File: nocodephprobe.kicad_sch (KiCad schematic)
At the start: 34 parts, among them J1 RF1-01 BNC, J2 10K, Q1 2N7002, U1 LMV358a, U2 ICL7106CPL, U3 MCP1501T-10E/CHY, U4 VI-302-DP-RC-S, U5 L7805

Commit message: Transpose R6 and R7
In the prototype the voffset was 0.3V instead of 0.7V!
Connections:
- net GND: now also R7.1; no longer R6.1
- net Voffset: now also R6.1, R7.2; no longer R6.2, R7.1
- net Vref: now also R6.2; no longer R7.2
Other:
- moved on the sheet: R6, R7
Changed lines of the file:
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@@
   (junction (at 142.24 64.77) (diameter 0) (color 0 0 0 0)
   )
+  (junction (at 68.58 142.24) (diameter 0) (color 0 0 0 0)
+  )
   (junction (at 69.85 74.93) (diameter 0) (color 0 0 0 0)
   )
   (junction (at 66.04 63.5) (diameter 0) (color 0 0 0 0)
-  )
-  (junction (at 68.58 142.24) (diameter 0) (color 0 0 0 0)
   )
   (junction (at 275.59 90.17) (diameter 0) (color 0 0 0 0)
@@
     (stroke (width 0) (type default))
   )
-  (wire (pts (xy 68.58 142.24) (xy 68.58 144.78))
-    (stroke (width 0) (type default))
-  )
   (wire (pts (xy 147.32 77.47) (xy 142.24 77.47))
     (stroke (width 0) (type default))
@@
     (stroke (width 0) (type default))
   )
+  (wire (pts (xy 68.58 142.24) (xy 68.58 143.51))
+    (stroke (width 0) (type default))
+  )
   (wire (pts (xy 222.25 86.36) (xy 222.25 90.17))
     (stroke (width 0) (type default))
@@
     (stroke (width 0) (type default))
   )
+  (wire (pts (xy 68.58 151.13) (xy 68.58 152.4))
+    (stroke (width 0) (type default))
+  )
   (wire (pts (xy 217.17 76.2) (xy 227.33 76.2))
     (stroke (width 0) (type default))
@@
   )
   (wire (pts (xy 224.79 85.09) (xy 240.03 85.09))
-    (stroke (width 0) (type default))
-  )
-  (wire (pts (xy 68.58 140.97) (xy 68.58 142.24))
     (stroke (width 0) (type default))
   )
@@
     )
   )
-  (symbol (lib_id "Device:R_US") (at 68.58 148.59 180) (unit 1)
+  (symbol (lib_id "Device:R_US") (at 68.58 138.43 180) (unit 1)
     (in_bom yes) (on_board yes) (dnp no)
-    (property "Reference" "R6" (at 71.12 148.59 0)
-      (effects (font (size 1.27 1.27)) (justify right))
-    )
-    (property "Value" "4.64k" (at 71.12 151.13 0)
-      (effects (font (size 1.27 1.27)) (justify right))
-    )
-    (property "Footprint" "Resistor_SMD:R_0805_2012Metric_Pad1.20x1.40mm_HandSolder" (at 67.564 148.336 90)
-      (effects (font (size 1.27 1.27)) hide)
-    )
-    (property "Datasheet" "~" (at 68.58 148.59 0)
-      (effects (font (size 1.27 1.27)) hide)
-    )
-    (property "Tolerance" "0.1%" (at 73.66 153.67 0)
+    (property "Reference" "R6" (at 71.12 138.43 0)
+      (effects (font (size 1.27 1.27)) (justify right))
+    )
+    (property "Value" "4.64k" (at 71.12 140.97 0)
+      (effects (font (size 1.27 1.27)) (justify right))
+    )
+    (property "Footprint" "Resistor_SMD:R_0805_2012Metric_Pad1.20x1.40mm_HandSolder" (at 67.564 138.176 90)
+      (effects (font (size 1.27 1.27)) hide)
+    )
+    (property "Datasheet" "~" (at 68.58 138.43 0)
+      (effects (font (size 1.27 1.27)) hide)
+    )
+    (property "Tolerance" "0.1%" (at 73.66 143.51 0)
       (effects (font (size 1.27 1.27)))
     )
@@
     )
   )
-  (symbol (lib_id "Device:R_US") (at 68.58 137.16 180) (unit 1)
+  (symbol (lib_id "Device:R_US") (at 68.58 147.32 180) (unit 1)
     (in_bom yes) (on_board yes) (dnp no)
-    (property "Reference" "R7" (at 71.12 137.16 0)
-      (effects (font (size 1.27 1.27)) (justify right))
-    )
-    (property "Value" "10k" (at 71.12 139.7 0)
-      (effects (font (size 1.27 1.27)) (justify right))
-    )
-    (property "Footprint" "Resistor_SMD:R_0805_2012Metric_Pad1.20x1.40mm_HandSolder" (at 67.564 136.906 90)
-      (effects (font (size 1.27 1.27)) hide)
-    )
-    (property "Datasheet" "~" (at 68.58 137.16 0)
-      (effects (font (size 1.27 1.27)) hide)
-    )
-    (property "Tolerance" "0.1%" (at 77.47 139.7 0)
-      (effects (font (size 1.27 1.27)))
-    )
-    (property "Field5" "" (at 68.58 137.16 0)
-      (effects (font (size 1.27 1.27)) hide)
-    )
+    (property "Reference" "R7" (at 71.12 147.32 0)
+      (effects (font (size 1.27 1.27)) (justify right))
+    )
+    (property "Value" "10k" (at 71.12 149.86 0)
+      (effects (font (size 1.27 1.27)) (justify right))
+    )
+    (property "Footprint" "Resistor_SMD:R_0805_2012Metric_Pad1.20x1.40mm_HandSolder" (at 67.564 147.066 90)
+      (effects (font (size 1.27 1.27)) hide)
+    )
+    (property "Datasheet" "~" (at 68.58 147.32 0)
+      (effects (font (size 1.27 1.27)) hide)
+    )
+    (property "Tolerance" "0.1%" (at 77.47 149.86 0)
+      (effects (font (size 1.27 1.27)))
+    )
+    (property "Field5" "" (at 68.58 147.32 0)
+      (effects (font (size 1.27 1.27)) hide)
+    )

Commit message: schematic: add pn and datasheet to ntc
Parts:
- J2: foot print pn (none) -> STX-3120-3B; pn (none) -> USP10982
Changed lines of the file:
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@@
       (effects (font (size 1.27 1.27)) hide)
     )
-    (property "Datasheet" "~" (at 152.4 68.58 0)
+    (property "Datasheet" "https://www.littelfuse.com/~/media/electronics/datasheets/thermistor_probes_and_assemblies/littelfuse_thermistor_probes_assemblies_plastic_usp10982_datasheet.pdf.pdf" (at 152.4 68.58 0)
       (effects (font (size 1.27 1.27)) hide)
     )
+    (property "pn" "USP10982" (at 152.4 69.85 0)
+      (effects (font (size 1.27 1.27)) hide)
+    )
+    (property "foot print pn" "STX-3120-3B" (at 152.4 69.85 0)
+      (effects (font (size 1.27 1.27)) hide)
+    )
+    (property "Field6" "" (at 152.4 69.85 0)
+      (effects (font (size 1.27 1.27)) hide)
+    )

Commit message: Add decoupling caps to potentiometers
This also changes the 7805 to a smaller footprint
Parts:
- added C10, C12: 0.1uF, Capacitor_SMD:C_0805_2012Metric_Pad1.18x1.45mm_HandSolder, symbol Device:C
- U5: value L7805 -> 78l05; footprint Package_TO_SOT_SMD:TO-252-3_TabPin2 -> Package_TO_SOT_SMD:SOT-89-3_Handsoldering; pn MC7805BDTRKG -> AS78L05RTR-E1
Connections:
- net -VDC: now also C10.1, C12.1
- net at J2.5, R1.1, RV2.1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: now also C12.2
- net at J1.2 (Ext), RV1.2: now also C10.2
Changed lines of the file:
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@@
   (junction (at 57.15 133.35) (diameter 0) (color 0 0 0 0)
   )
+  (junction (at 147.32 77.47) (diameter 0) (color 0 0 0 0)
+  )
+  (junction (at 85.09 100.33) (diameter 0) (color 0 0 0 0)
+  )
   (junction (at 172.72 38.1) (diameter 0) (color 0 0 0 0)
   )
+  (junction (at 153.67 100.33) (diameter 0) (color 0 0 0 0)
+  )
   (junction (at 142.24 86.36) (diameter 0) (color 0 0 0 0)
   )
@@
   )
   (junction (at 34.29 66.04) (diameter 0) (color 0 0 0 0)
+  )
+  (junction (at 85.09 66.04) (diameter 0) (color 0 0 0 0)
   )
   (junction (at 68.58 133.35) (diameter 0) (color 0 0 0 0)
@@
     (stroke (width 0) (type default))
   )
+  (wire (pts (xy 153.67 77.47) (xy 147.32 77.47))
+    (stroke (width 0) (type default))
+  )
   (wire (pts (xy 124.46 35.56) (xy 124.46 54.61))
     (stroke (width 0) (type default))
@@
     (stroke (width 0) (type default))
   )
-  (wire (pts (xy 66.04 100.33) (xy 124.46 100.33))
+  (wire (pts (xy 66.04 100.33) (xy 85.09 100.33))
     (stroke (width 0) (type default))
   )
@@
     (stroke (width 0) (type default))
   )
+  (wire (pts (xy 85.09 66.04) (xy 107.95 66.04))
+    (stroke (width 0) (type default))
+  )
+  (wire (pts (xy 153.67 100.33) (xy 201.93 100.33))
+    (stroke (width 0) (type default))
+  )
   (wire (pts (xy 66.04 83.82) (xy 66.04 100.33))
     (stroke (width 0) (type default))
@@
     (stroke (width 0) (type default))
   )
+  (wire (pts (xy 153.67 85.09) (xy 153.67 77.47))
+    (stroke (width 0) (type default))
+  )
   (wire (pts (xy 66.04 53.34) (xy 66.04 54.61))
     (stroke (width 0) (type default))
@@
     (stroke (width 0) (type default))
   )
+  (wire (pts (xy 85.09 85.09) (xy 85.09 100.33))
+    (stroke (width 0) (type default))
+  )
   (wire (pts (xy 45.72 124.46) (xy 45.72 125.73))
     (stroke (width 0) (type default))
@@
     (stroke (width 0) (type default))
   )
+  (wire (pts (xy 85.09 100.33) (xy 124.46 100.33))
+    (stroke (width 0) (type default))
+  )
   (wire (pts (xy 231.14 35.56) (xy 217.17 35.56))
     (stroke (width 0) (type default))
@@
     (stroke (width 0) (type default))
   )
+  (wire (pts (xy 153.67 92.71) (xy 153.67 100.33))
+    (stroke (width 0) (type default))
+  )
   (wire (pts (xy 238.76 52.07) (xy 240.03 52.07))
     (stroke (width 0) (type default))
@@
     (stroke (width 0) (type default))
   )
-  (wire (pts (xy 81.28 66.04) (xy 107.95 66.04))
+  (wire (pts (xy 81.28 66.04) (xy 85.09 66.04))
     (stroke (width 0) (type default))
   )
@@
     (stroke (width 0) (type default))
   )
-  (wire (pts (xy 124.46 100.33) (xy 201.93 100.33))
+  (wire (pts (xy 124.46 100.33) (xy 153.67 100.33))
     (stroke (width 0) (type default))
   )
@@
   )
   (wire (pts (xy 113.03 46.99) (xy 101.6 46.99))
+    (stroke (width 0) (type default))
+  )
+  (wire (pts (xy 85.09 66.04) (xy 85.09 77.47))
     (stroke (width 0) (type default))
   )
@@
     (effects (font (size 0.889 0.889)) (justify left bottom))
   )
-  (text "C5 should be\npolypropylene" (at 157.48 95.25 0)
+  (text "C5 should be\npolypropylene" (at 162.56 99.06 0)
     (effects (font (size 1.27 1.27)) (justify left bottom))
   )
@@
       (effects (font (size 1.27 1.27)))
     )
-    (property "Value" "L7805" (at 113.03 31.75 0)
-      (effects (font (size 1.27 1.27)))
-    )
-    (property "Footprint" "Package_TO_SOT_SMD:TO-252-3_TabPin2" (at 113.665 39.37 0)
+    (property "Value" "78l05" (at 113.03 31.75 0)
+      (effects (font (size 1.27 1.27)))
+    )
+    (property "Footprint" "Package_TO_SOT_SMD:SOT-89-3_Handsoldering" (at 113.665 39.37 0)
       (effects (font (size 1.27 1.27) italic) (justify left) hide)
     )
-    (property "Datasheet" "http://www.st.com/content/ccc/resource/technical/document/datasheet/41/4f/b3/b0/12/d4/47/88/CD00000444.pdf/files/CD00000444.pdf/jcr:content/translations/en.CD00000444.pdf" (at 113.03 36.83 0)
-      (effects (font (size 1.27 1.27)) hide)
-    )
-    (property "pn" "MC7805BDTRKG" (at 113.03 35.56 0)
+    (property "Datasheet" "https://media.digikey.com/pdf/Data%20Sheets/Diodes%20PDFs/AS78Lxx_Aug2013_DS.pdf" (at 113.03 36.83 0)
+      (effects (font (size 1.27 1.27)) hide)
+    )
+    (property "pn" "AS78L05RTR-E1" (at 113.03 35.56 0)
       (effects (font (size 1.27 1.27)) hide)
     )
@@
         (path "/2036f74b-8ede-4e4d-84df-8cc119de9ab1"
           (reference "#PWR014") (unit 1)
+        )
+      )
+    )
+  )
+  (symbol (lib_id "Device:C") (at 153.67 88.9 180) (unit 1)
+    (in_bom yes) (on_board yes) (dnp no) (fields_autoplaced)
+    (property "Reference" "C12" (at 157.48 87.63 0)
+      (effects (font (size 1.27 1.27)) (justify right))
+    )
+    (property "Value" "0.1uF" (at 157.48 90.17 0)
+      (effects (font (size 1.27 1.27)) (justify right))
+    )
+    (property "Footprint" "Capacitor_SMD:C_0805_2012Metric_Pad1.18x1.45mm_HandSolder" (at 152.7048 85.09 0)
+      (effects (font (size 1.27 1.27)) hide)
+    )
+    (property "Datasheet" "~" (at 153.67 88.9 0)
+      (effects (font (size 1.27 1.27)) hide)
+    )
+    (pin "1")
+    (pin "2")
+    (instances
+      (project "nocodephprobe"
+        (path "/2036f74b-8ede-4e4d-84df-8cc119de9ab1"
+          (reference "C12") (unit 1)
         )
       )
@@
         )
       )
+    )
+  )
+  (symbol (lib_id "Device:C") (at 85.09 81.28 180) (unit 1)
+    (in_bom yes) (on_board yes) (dnp no) (fields_autoplaced)
+    (property "Reference" "C10" (at 88.9 80.01 0)
+      (effects (font (size 1.27 1.27)) (justify right))
+    )
+    (property "Value" "0.1uF" (at 88.9 82.55 0)
+      (effects (font (size 1.27 1.27)) (justify right))
+    )
+    (property "Footprint" "Capacitor_SMD:C_0805_2012Metric_Pad1.18x1.45mm_HandSolder" (at 84.1248 77.47 0)
+      (effects (font (size 1.27 1.27)) hide)
+    )
+    (property "Datasheet" "~" (at 85.09 81.28 0)
+      (effects (font (size 1.27 1.27)) hide)
+    )
+    (pin "1")
+    (pin "2")
+    (instances
+      (project "nocodephprobe"
+        (path "/2036f74b-8ede-4e4d-84df-8cc119de9ab1"
+          (reference "C10") (unit 1)
+        )
+      )

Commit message: Change D1 to a Schottky diode
This will reduce the range of the zero calibration from +/- 0.3V to +/-
0.15V and make the setting less finicky.
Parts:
- D1: value 1N4148W -> SS14; footprint Diode_SMD:D_SOD-123 -> Diode_SMD:D_SMA; symbol Diode:1N4148W -> Device:D_Schottky
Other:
- note added: "-0.15V to +0.15V"
- note removed: "-0.3V to +0.3V"
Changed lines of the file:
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@@
     (effects (font (size 1.27 1.27)) (justify left bottom))
   )
-  (text "-0.3V to\n+0.3V" (at 88.9 64.77 0)
+  (text "-0.15V to\n+0.15V" (at 88.9 64.77 0)
     (effects (font (size 1.27 1.27)) (justify left bottom))
   )
@@
     )
   )
-  (symbol (lib_id "Diode:1N4148W") (at 69.85 63.5 90) (unit 1)
+  (symbol (lib_id "Device:D_Schottky") (at 69.85 63.5 90) (unit 1)
     (in_bom yes) (on_board yes) (dnp no)
     (property "Reference" "D1" (at 71.12 59.69 90)
       (effects (font (size 1.27 1.27)) (justify right))
     )
-    (property "Value" "1N4148W" (at 72.39 62.23 0)
-      (effects (font (size 1.27 1.27)) (justify right))
-    )
-    (property "Footprint" "Diode_SMD:D_SOD-123" (at 74.295 63.5 0)
-      (effects (font (size 1.27 1.27)) hide)
-    )
-    (property "Datasheet" "https://www.vishay.com/docs/85748/1n4148w.pdf" (at 69.85 63.5 0)
-      (effects (font (size 1.27 1.27)) hide)
-    )
+    (property "Value" "SS14" (at 72.39 62.23 0)
+      (effects (font (size 1.27 1.27)) (justify right) hide)
+    )
+    (property "Footprint" "Diode_SMD:D_SMA" (at 69.85 63.5 0)
+      (effects (font (size 1.27 1.27)) hide)
+    )
+    (property "Datasheet" "~" (at 69.85 63.5 0)
+      (effects (font (size 1.27 1.27)) hide)
+    )

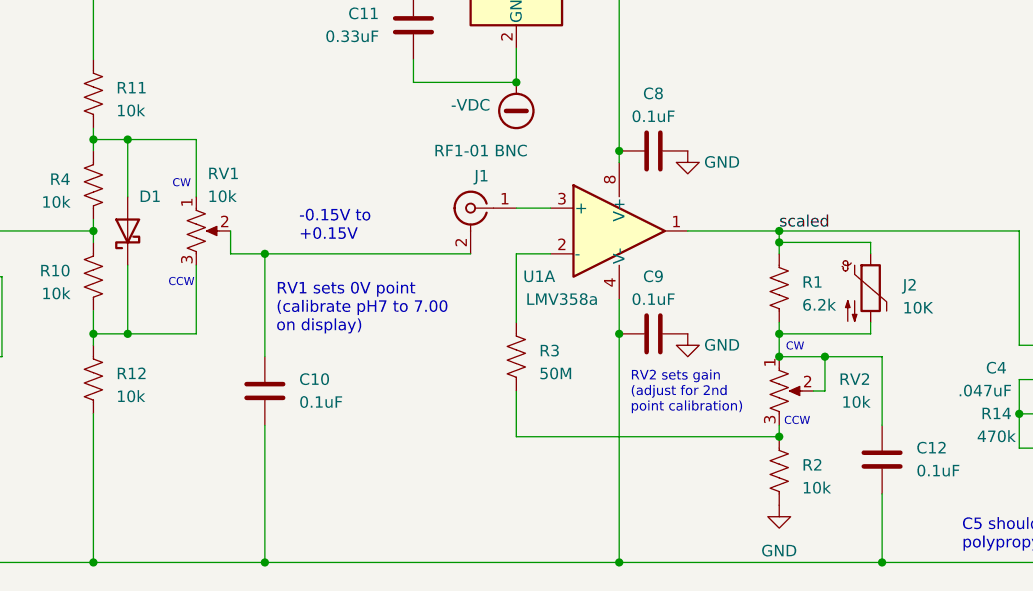
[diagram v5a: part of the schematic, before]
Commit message: Flip pots so that CW increases pH during calibration
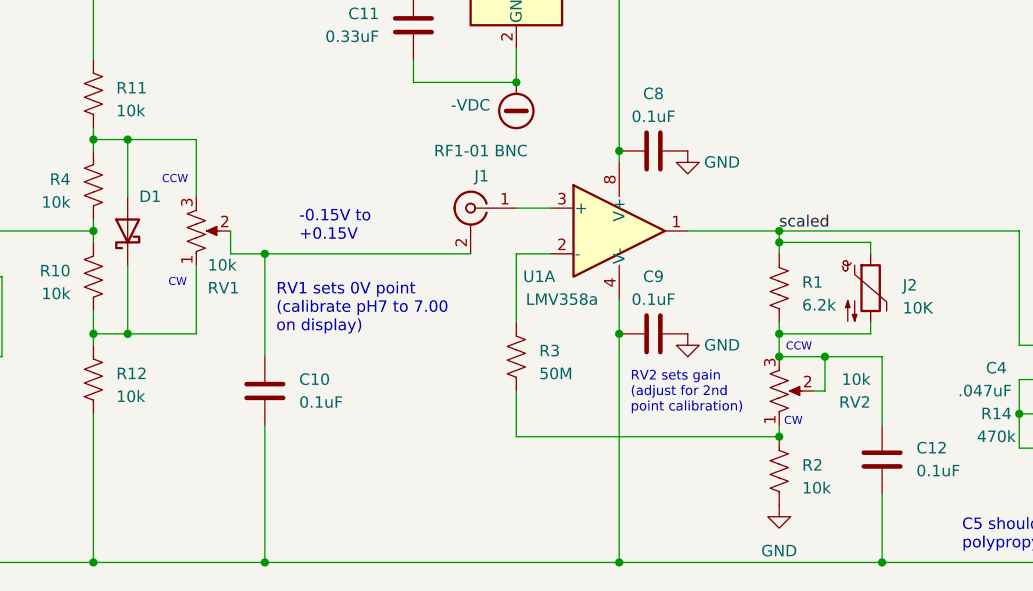
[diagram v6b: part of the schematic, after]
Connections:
- net at R2.2, R3.2: now also RV2.1; no longer RV2.3
- net at C12.2, J2.5, R1.1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: now also RV2.3; no longer RV2.1
- net at D1.1 (K), R10.1, R12.2: now also RV1.1; no longer RV1.3
- net at D1.2 (A), R11.1, R4.2: now also RV1.3; no longer RV1.1
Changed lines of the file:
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@@
     (stroke (width 0) (type default))
   )
-  (text "CCW" (at 74.3724 69.8624 0)
+  (text "CW" (at 74.3724 69.8624 0)
     (effects (font (size 0.889 0.889)) (justify left bottom))
   )
@@
     (effects (font (size 1.27 1.27)) (justify left bottom))
   )
-  (text "CCW" (at 142.7857 85.2966 0)
+  (text "CW" (at 142.7857 85.2966 0)
     (effects (font (size 0.889 0.889)) (justify left bottom))
   )
@@
     (effects (font (size 1.27 1.27)) (justify left bottom))
   )
-  (text "CW" (at 142.9793 77.0231 0)
+  (text "CCW" (at 142.9793 77.0231 0)
     (effects (font (size 0.889 0.889)) (justify left bottom))
   )
-  (text "CW" (at 74.8198 58.8836 0)
+  (text "CCW" (at 73.66 58.42 0)
     (effects (font (size 0.889 0.889)) (justify left bottom))
   )
@@
     )
   )
-  (symbol (lib_id "Device:R_Potentiometer_US") (at 142.24 81.28 0) (unit 1)
-    (in_bom yes) (on_board yes) (dnp no)
-    (property "Reference" "RV2" (at 152.4 80.01 0)
-      (effects (font (size 1.27 1.27)) (justify right))
-    )
-    (property "Value" "10k" (at 152.4 82.55 0)
+  (symbol (lib_id "Device:R_Potentiometer_US") (at 142.24 81.28 0) (mirror x) (unit 1)
+    (in_bom yes) (on_board yes) (dnp no)
+    (property "Reference" "RV2" (at 152.4 82.55 0)
+      (effects (font (size 1.27 1.27)) (justify right))
+    )
+    (property "Value" "10k" (at 152.4 80.01 0)
       (effects (font (size 1.27 1.27)) (justify right))
     )
@@
     )
   )
-  (symbol (lib_id "Device:R_Potentiometer_US") (at 77.47 63.5 0) (unit 1)
-    (in_bom yes) (on_board yes) (dnp no)
-    (property "Reference" "RV1" (at 78.74 57.15 0)
+  (symbol (lib_id "Device:R_Potentiometer_US") (at 77.47 63.5 0) (mirror x) (unit 1)
+    (in_bom yes) (on_board yes) (dnp no)
+    (property "Reference" "RV1" (at 78.74 69.85 0)
       (effects (font (size 1.27 1.27)) (justify left))
     )
-    (property "Value" "10k" (at 78.74 59.69 0)
+    (property "Value" "10k" (at 78.74 67.31 0)
       (effects (font (size 1.27 1.27)) (justify left))
     )

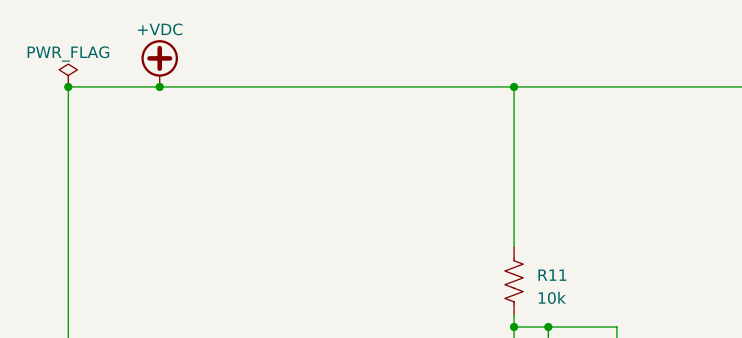
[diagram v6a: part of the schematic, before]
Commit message: Add header for power switch
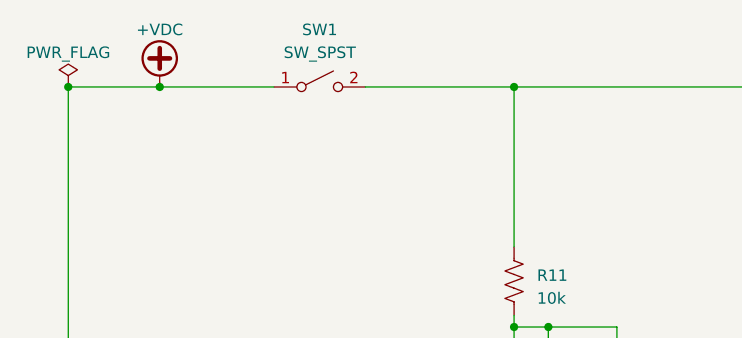
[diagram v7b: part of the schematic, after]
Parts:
- added SW1: SW_SPST, Connector_PinHeader_2.54mm:PinHeader_2x01_P2.54mm_Vertical, symbol Switch:SW_SPST
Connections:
- net +VDC: now also SW1.1 (A); no longer C11.2, C6.1, R11.2, U2.1 (V+), U5.1 (IN)
- new net: C11.2, C6.1, R11.2, SW1.2 (B), U2.1 (V+), U5.1 (IN)
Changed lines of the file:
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@@
+    (stroke (width 0) (type default))
+  )
+  (wire (pts (xy 49.53 26.67) (xy 66.04 26.67))
     (stroke (width 0) (type default))
   )
@@
     (stroke (width 0) (type default))
   )
-  (wire (pts (xy 26.67 26.67) (xy 66.04 26.67))
+  (wire (pts (xy 26.67 26.67) (xy 39.37 26.67))
     (stroke (width 0) (type default))
   )
@@
         )
       )
+    )
+  )
+  (symbol (lib_id "Switch:SW_SPST") (at 44.45 26.67 0) (unit 1)
+    (in_bom yes) (on_board yes) (dnp no) (fields_autoplaced)
+    (property "Reference" "SW1" (at 44.45 20.32 0)
+      (effects (font (size 1.27 1.27)))
+    )
+    (property "Value" "SW_SPST" (at 44.45 22.86 0)
+      (effects (font (size 1.27 1.27)))
+    )
+    (property "Footprint" "Connector_PinHeader_2.54mm:PinHeader_2x01_P2.54mm_Vertical" (at 44.45 26.67 0)
+      (effects (font (size 1.27 1.27)) hide)
+    )
+    (property "Datasheet" "~" (at 44.45 26.67 0)
+      (effects (font (size 1.27 1.27)) hide)
+    )
+    (pin "1")
+    (pin "2")
+    (instances
+      (project "nocodephprobe"
+        (path "/2036f74b-8ede-4e4d-84df-8cc119de9ab1"
+          (reference "SW1") (unit 1)
+        )
+      )
